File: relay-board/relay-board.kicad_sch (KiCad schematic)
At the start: 69 parts, among them J1 Conn_01x02, J2 Conn_01x02, J3 Conn_01x02, J4 Conn_01x02, J5 Conn_01x02, J6 Conn_01x02, J7 Conn_01x02, J8 Conn_01x02, J9 Conn_01x25, Q1 PN2222ATA, Q2 PN2222ATA, Q3 PN2222ATA, Q4 PN2222ATA, Q5 PN2222ATA, Q6 PN2222ATA, Q7 PN2222ATA, Q8 PN2222ATA, U1 FOD814A, U10 RTD14005, U11 FOD814A, U12 RTD14005, U13 FOD814A, U14 RTD14005, U15 FOD814A, U16 RTD14005, U2 RTD14005, U3 FOD814A, U4 RTD14005, U5 FOD814A, U6 RTD14005, U7 FOD814A, U8 RTD14005, U9 FOD814A

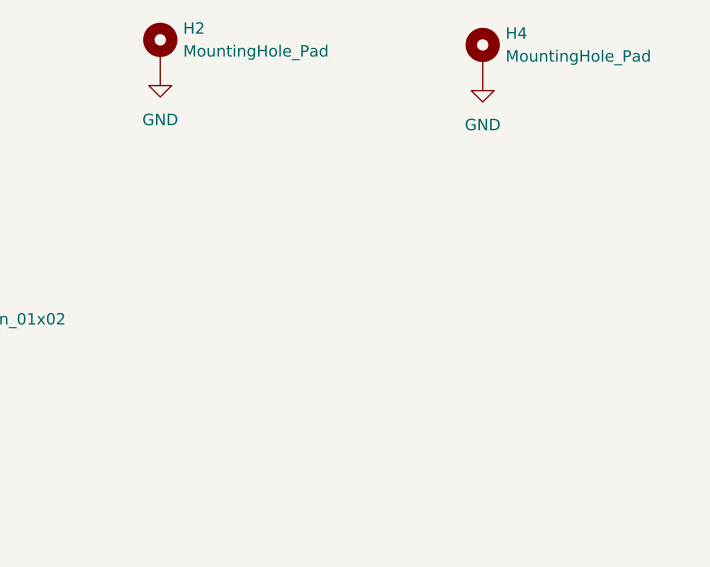
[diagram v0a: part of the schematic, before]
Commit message: relay-board: rename project and update to KiCad 10
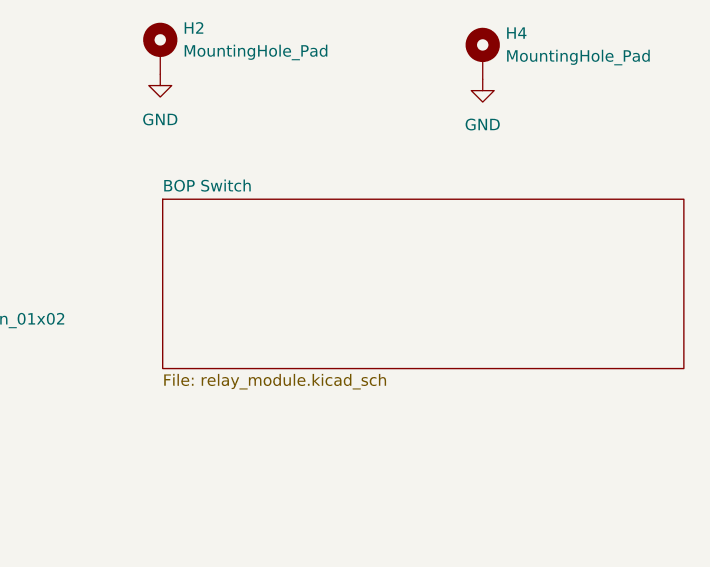
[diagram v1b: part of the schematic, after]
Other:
- added sheet BOP Switch (relay_module.kicad_sch)

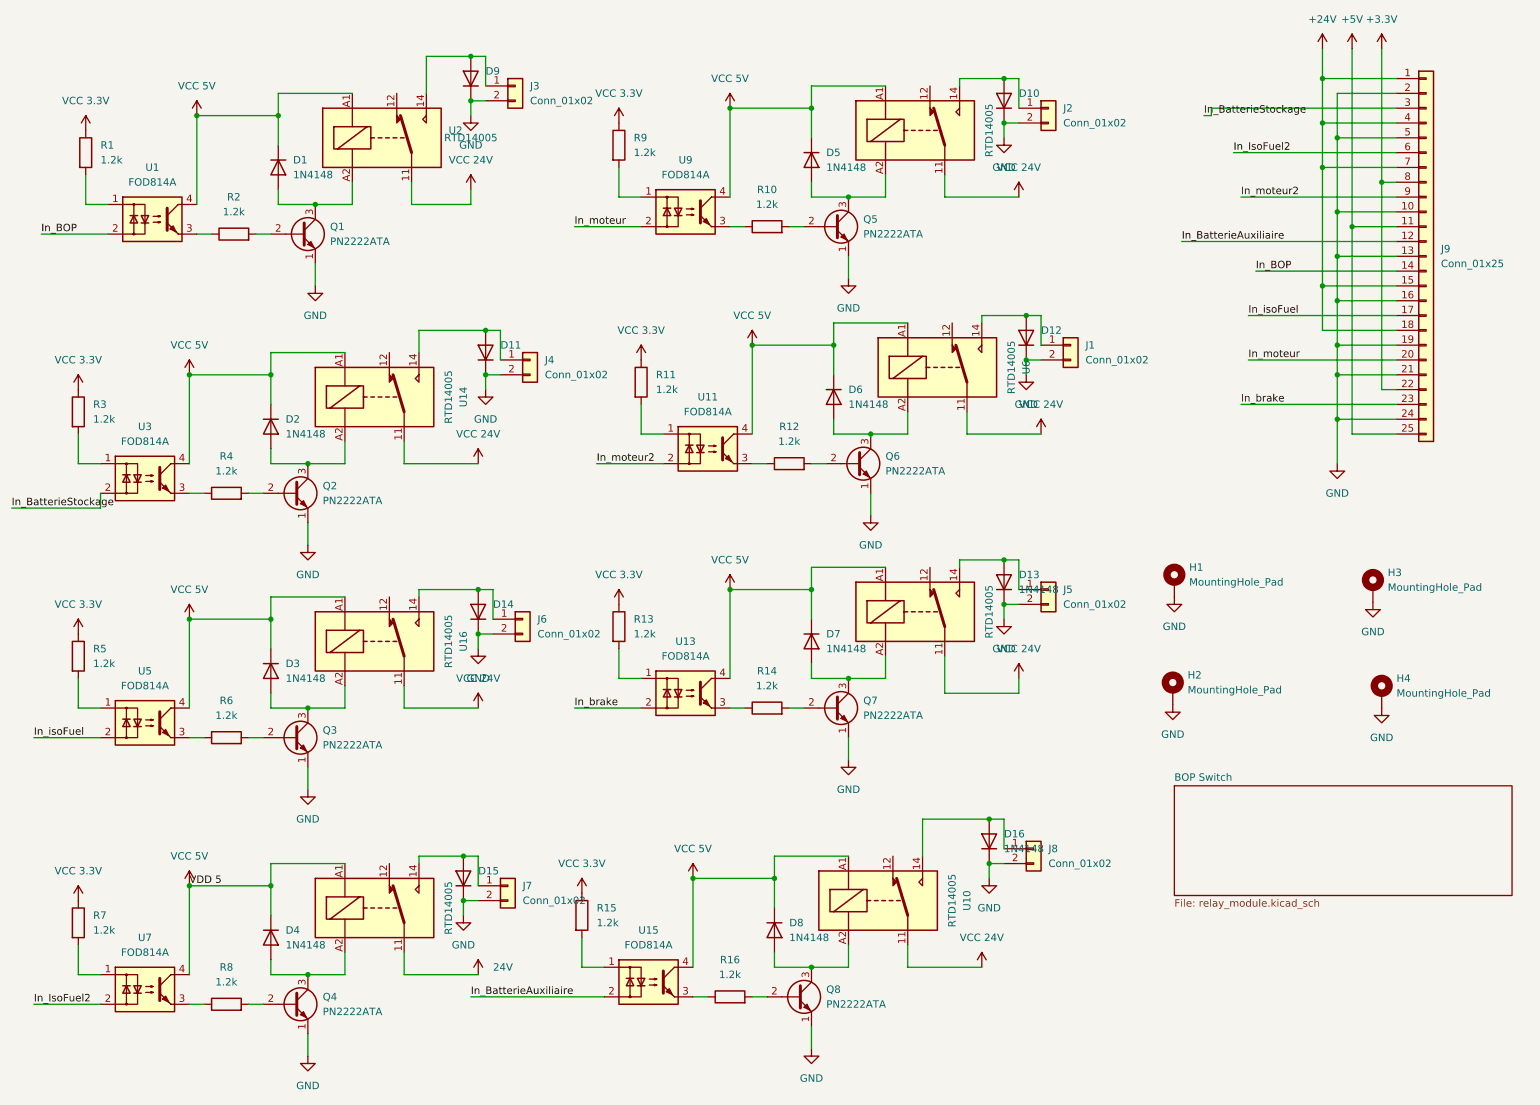
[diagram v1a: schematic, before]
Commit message: relay-board: split schematic into pages
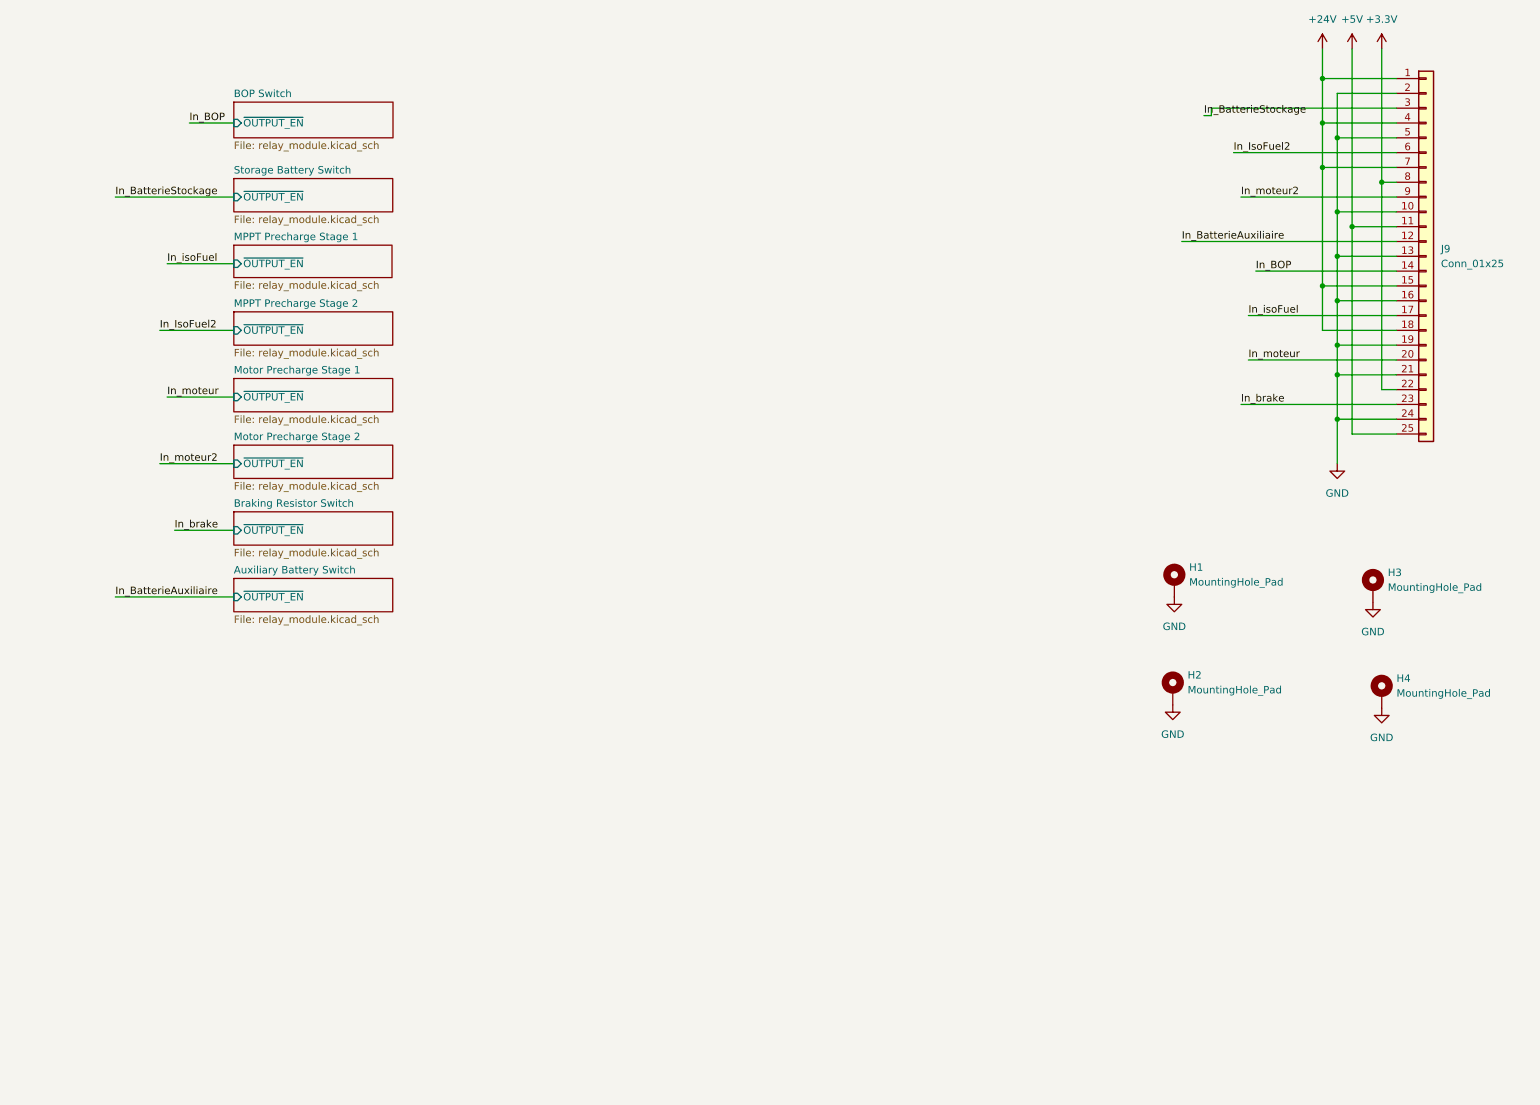
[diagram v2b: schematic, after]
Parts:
- removed D1, D10, D11, D12, D13, D14, D15, D16, D2, D3, D4, D5, D6, D7, D8, D9: 1N4148, Diode_THT:D_DO-35_SOD27_P7.62mm_Horizontal, symbol Diode:1N4148
- removed J1, J2, J3, J4, J5, J6, J7, J8: Conn_01x02, TerminalBlock:TerminalBlock_MaiXu_MX126-5.0-02P_1x02_P5.00mm, symbol Connector_Generic:Conn_01x02
- removed Q1, Q2, Q3, Q4, Q5, Q6, Q7, Q8: PN2222ATA, Package_TO_SOT_THT:TO-92_Inline, symbol Transistor_BJT:PN2222A
- removed R1, R10, R11, R12, R13, R14, R15, R16, R2, R3, R4, R5, R6, R7, R8, R9: 1.2k, Resistor_THT:R_Axial_DIN0309_L9.0mm_D3.2mm_P12.70mm_Horizontal, symbol Device:R
- removed U1, U11, U13, U15, U3, U5, U7, U9: FOD814A, Package_DIP:DIP-4_W7.62mm, symbol Isolator:LTV-814
- removed U10, U12, U14, U16, U2, U4, U6, U8: RTD14005, Relay_THT:Relay_DPDT_Schrack-RT2-FormC_RM5mm, symbol Relay:RT314A05
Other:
- added sheet Auxiliary Battery Switch (relay_module.kicad_sch)
- added sheet Braking Resistor Switch (relay_module.kicad_sch)
- added sheet MPPT Precharge Stage 1 (relay_module.kicad_sch)
- added sheet MPPT Precharge Stage 2 (relay_module.kicad_sch)
- added sheet Motor Precharge Stage 1 (relay_module.kicad_sch)
- added sheet Motor Precharge Stage 2 (relay_module.kicad_sch)
- added sheet Storage Battery Switch (relay_module.kicad_sch)
- sheet BOP Switch ports: added ~{OUTPUT_EN}; removed none

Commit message: relay-board: update drawing sheet and metadata
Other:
- title: (none) -> Main page

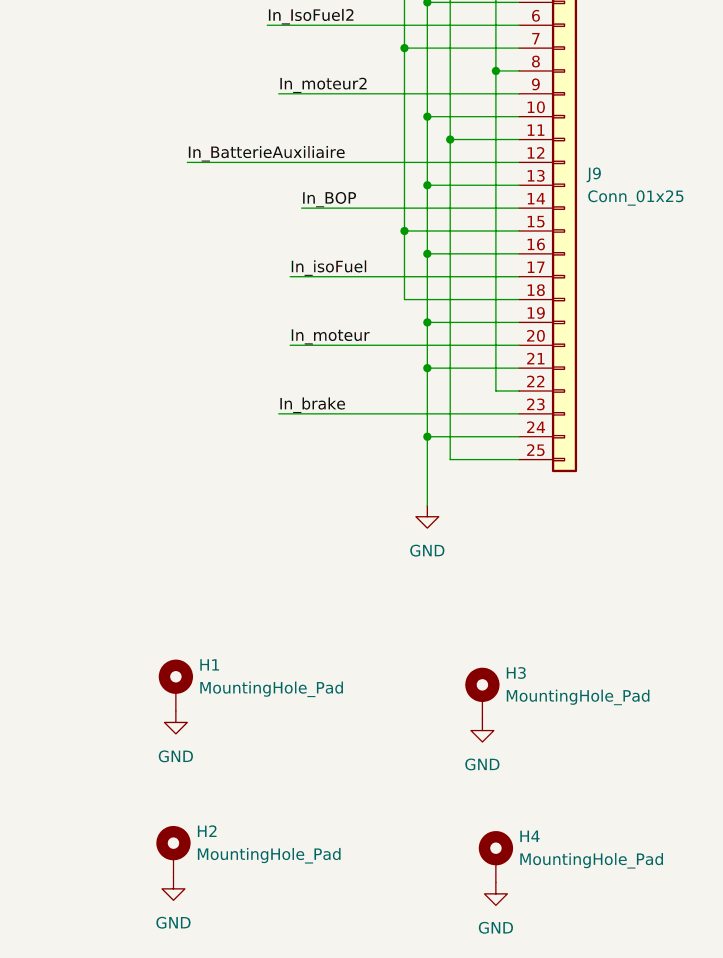
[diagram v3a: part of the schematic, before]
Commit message: relay-board: add screw terminal footprint
Also re-annotated schematic because page 3 had issues.
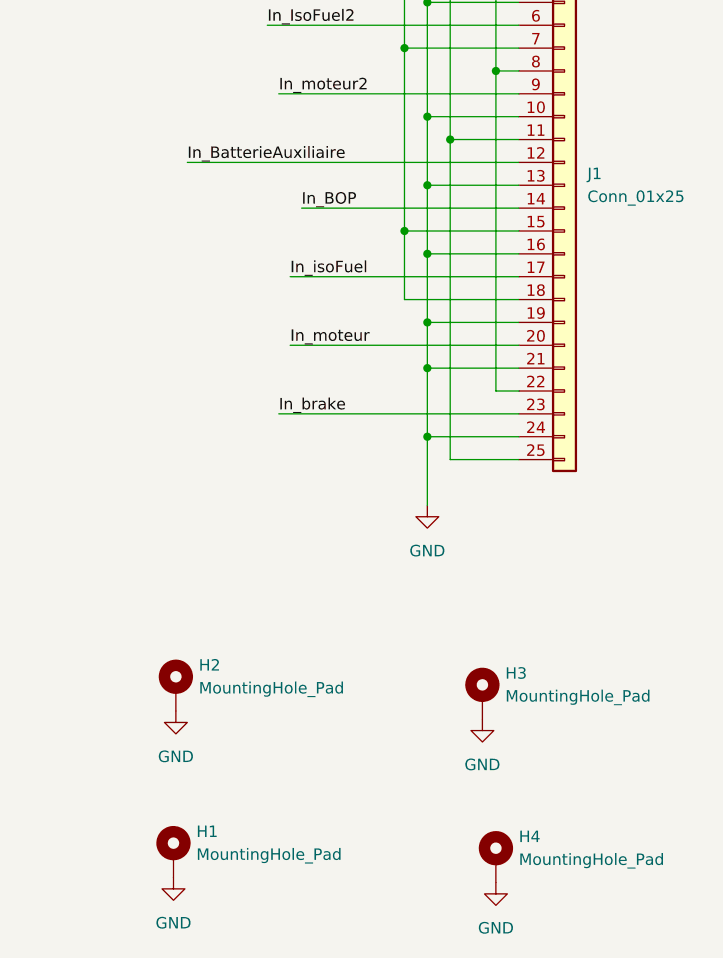
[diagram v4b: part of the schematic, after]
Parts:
- renumbered H2 to H1, H1 to H2, J9 to J1
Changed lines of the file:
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@@
 		(dnp no)
 		(fields_autoplaced yes)
-		(property "Reference" "H2"
+		(property "Reference" "H1"
 			(at 214.3627 127.7074 0)
 			(show_name no)
@@
 			(project "relay-board"
 				(path "/35014b8f-a7d4-4398-be8d-6f1338f2031d"
-					(reference "H2")
+					(reference "H1")
 					(unit 1)
 				)
@@
 		(dnp no)
 		(fields_autoplaced yes)
-		(property "Reference" "#PWR018"
+		(property "Reference" "#PWR01"
 			(at 211.8227 139.1375 0)
 			(hide yes)
@@
 			(project "relay-board"
 				(path "/35014b8f-a7d4-4398-be8d-6f1338f2031d"
-					(reference "#PWR018")
+					(reference "#PWR01")
 					(unit 1)
 				)
@@
 		(dnp no)
 		(fields_autoplaced yes)
-		(property "Reference" "H1"
+		(property "Reference" "H2"
 			(at 214.63 109.2199 0)
 			(show_name no)
@@
 			(project "relay-board"
 				(path "/35014b8f-a7d4-4398-be8d-6f1338f2031d"
-					(reference "H1")
+					(reference "H2")
 					(unit 1)
 				)
@@
 		(dnp no)
 		(fields_autoplaced yes)
-		(property "Reference" "#PWR024"
+		(property "Reference" "#PWR05"
 			(at 242.57 24.13 0)
 			(hide yes)
@@
 			(project "relay-board"
 				(path "/35014b8f-a7d4-4398-be8d-6f1338f2031d"
-					(reference "#PWR024")
+					(reference "#PWR05")
 					(unit 1)
 				)
@@
 		(dnp no)
 		(fields_autoplaced yes)
-		(property "Reference" "#PWR017"
+		(property "Reference" "#PWR02"
 			(at 212.09 120.65 0)
 			(hide yes)
@@
 			(project "relay-board"
 				(path "/35014b8f-a7d4-4398-be8d-6f1338f2031d"
-					(reference "#PWR017")
+					(reference "#PWR02")
 					(unit 1)
 				)
@@
 		(dnp no)
 		(fields_autoplaced yes)
-		(property "Reference" "#PWR021"
+		(property "Reference" "#PWR03"
 			(at 237.49 24.13 0)
 			(hide yes)
@@
 			(project "relay-board"
 				(path "/35014b8f-a7d4-4398-be8d-6f1338f2031d"
-					(reference "#PWR021")
+					(reference "#PWR03")
 					(unit 1)
 				)
@@
 		(dnp no)
 		(fields_autoplaced yes)
-		(property "Reference" "#PWR027"
+		(property "Reference" "#PWR07"
 			(at 247.65 24.13 0)
 			(hide yes)
@@
 			(project "relay-board"
 				(path "/35014b8f-a7d4-4398-be8d-6f1338f2031d"
-					(reference "#PWR027")
+					(reference "#PWR07")
 					(unit 1)
 				)
@@
 		(dnp no)
 		(fields_autoplaced yes)
-		(property "Reference" "#PWR020"
+		(property "Reference" "#PWR08"
 			(at 247.65 139.7 0)
 			(hide yes)
@@
 			(project "relay-board"
 				(path "/35014b8f-a7d4-4398-be8d-6f1338f2031d"
-					(reference "#PWR020")
+					(reference "#PWR08")
 					(unit 1)
 				)
@@
 		(dnp no)
 		(fields_autoplaced yes)
-		(property "Reference" "#PWR019"
+		(property "Reference" "#PWR06"
 			(at 246.147 121.5498 0)
 			(hide yes)
@@
 			(project "relay-board"
 				(path "/35014b8f-a7d4-4398-be8d-6f1338f2031d"
-					(reference "#PWR019")
+					(reference "#PWR06")
 					(unit 1)
 				)
@@
 		(dnp no)
 		(fields_autoplaced yes)
-		(property "Reference" "J9"
+		(property "Reference" "J1"
 			(at 257.81 54.6099 0)
 			(show_name no)
@@
 			(project "relay-board"
 				(path "/35014b8f-a7d4-4398-be8d-6f1338f2031d"
-					(reference "J9")
+					(reference "J1")
 					(unit 1)
 				)
@@
 		(dnp no)
 		(fields_autoplaced yes)
-		(property "Reference" "#PWR030"
+		(property "Reference" "#PWR04"
 			(at 240.03 97.79 0)
 			(hide yes)
@@
 			(project "relay-board"
 				(path "/35014b8f-a7d4-4398-be8d-6f1338f2031d"
-					(reference "#PWR030")
-					(unit 1)
-				)
+					(reference "#PWR04")
+					(unit 1)
+				)
